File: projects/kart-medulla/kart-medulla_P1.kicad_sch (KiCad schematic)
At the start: 67 parts, among them CN1 1990012, CN10 1990012, CN2 1990012, CN3 1990012, CN4 1990012, CN5 1990012, CN6 1990012, CN7 1990012, CN8 1990012, CN9 1990012, Q3 IRLZ44NPBF, Q4 BSS123_C5184436, U1 LM358DR, U13 MCP4922-E/SL, U14 MAX4660EUA+T, U19 L7805CDT_C20611927, U23 SSW-122-01-T-D, U24 SSW-122-01-T-S, U25 PCF8574T/3,518, U5 SN74LVC3G17DCTR

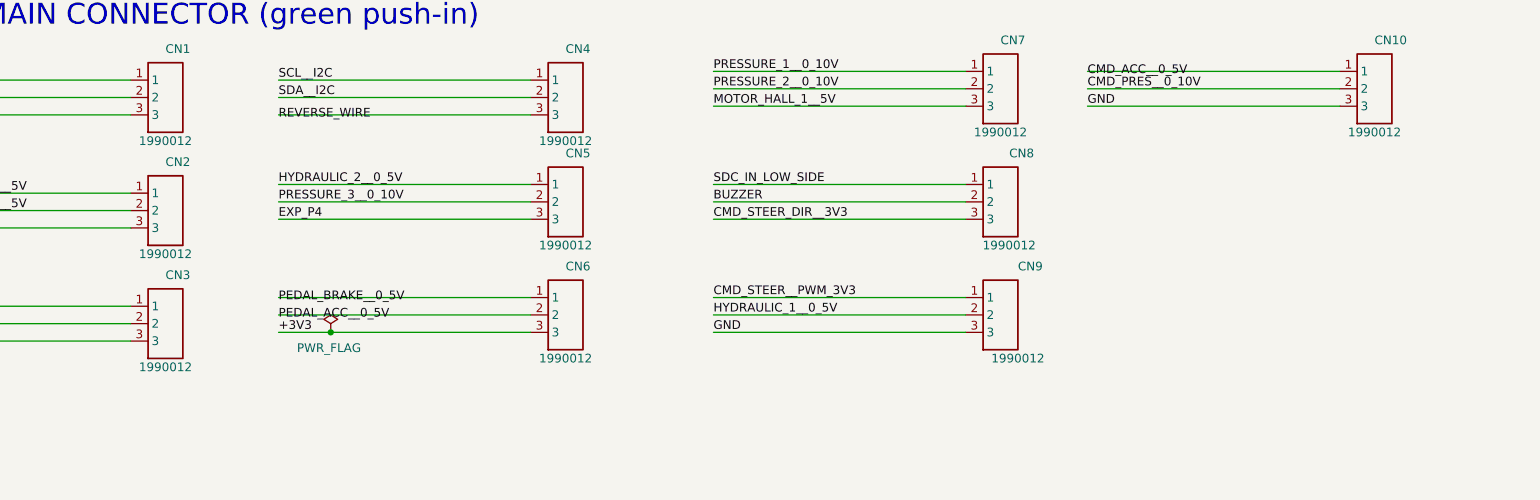
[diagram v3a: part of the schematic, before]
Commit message: swap all ten connectors to the WAGO 2601-3103
CN1-CN10 now use TerminalBlock_WAGO:TerminalBlock_WAGO_2601-3103_1x03_P3.50mm_Vertical
with Value 2601-3103. One connector family, 17.5 A against the Phoenix part's 2 A, top
entry so wires leave upward.

A blind string replace also hit the schematic's cached lib_symbols copy of the symbol,
which made ERC report ten lib_symbol_mismatch warnings because the cache no longer matched
kart-medulla.kicad_sym. Only placed instances carry the new Value; the cached symbol keeps
matching the master. Reverted that one field, ERC back to 0.

The symbol is still named 1990012 after the part it no longer represents - left alone,
since renaming touches the master, the cache and every instance for no electrical gain.

The PCB still has the Phoenix footprints, so parity reports ten more mismatches until the
re-layout.
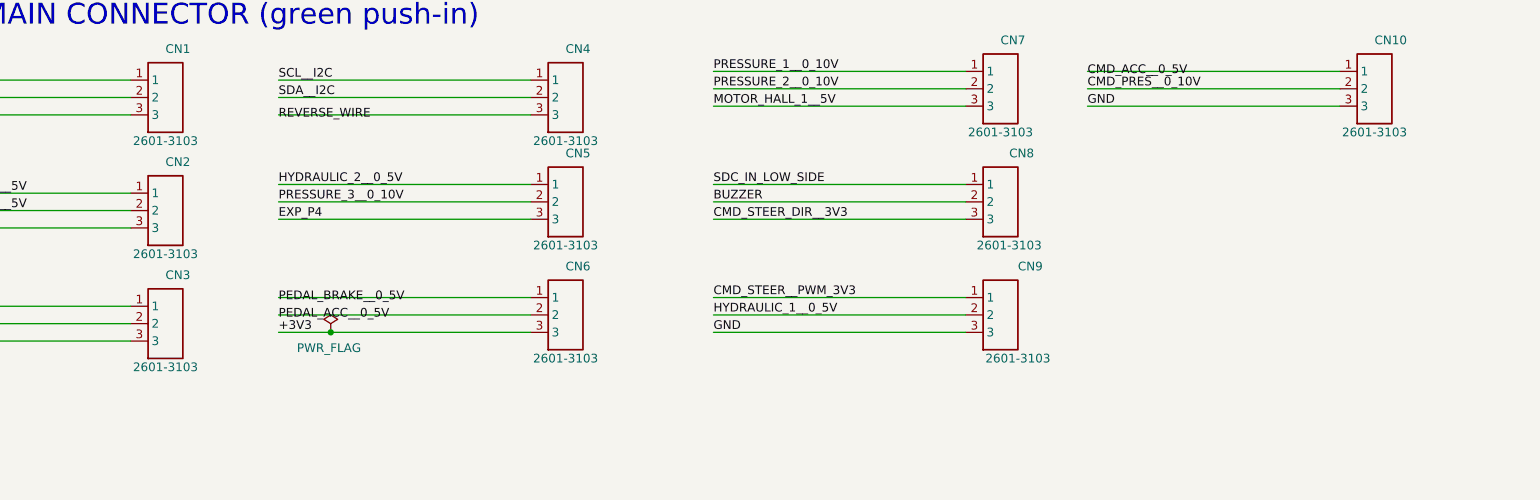
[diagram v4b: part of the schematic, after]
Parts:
- CN1, CN10, CN2, CN3, CN4, CN5, CN6, CN7, CN8, CN9: value 1990012 -> 2601-3103; footprint kart-medulla:CONN-TH_3P-P2.50-S5.00_1990012 -> TerminalBlock_WAGO:TerminalBlock_WAGO_2601-3103_1x03_P3.50mm_Vertical
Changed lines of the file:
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@@
 			)
 		)
-		(property "Value" "1990012"
+		(property "Value" "2601-3103"
 			(at 83.82 72.39 0)
 			(show_name no)
@@
 			)
 		)
-		(property "Footprint" "kart-medulla:CONN-TH_3P-P2.50-S5.00_1990012"
+		(property "Footprint" "TerminalBlock_WAGO:TerminalBlock_WAGO_2601-3103_1x03_P3.50mm_Vertical"
 			(at 83.82 66.04 0)
 			(hide yes)
@@
 			)
 		)
-		(property "Value" "1990012"
+		(property "Value" "2601-3103"
 			(at 83.82 55.88 0)
 			(show_name no)
@@
 			)
 		)
-		(property "Footprint" "kart-medulla:CONN-TH_3P-P2.50-S5.00_1990012"
+		(property "Footprint" "TerminalBlock_WAGO:TerminalBlock_WAGO_2601-3103_1x03_P3.50mm_Vertical"
 			(at 83.82 49.53 0)
 			(hide yes)
@@
 			)
 		)
-		(property "Value" "1990012"
+		(property "Value" "2601-3103"
 			(at 208.28 87.63 0)
 			(show_name no)
@@
 			)
 		)
-		(property "Footprint" "kart-medulla:CONN-TH_3P-P2.50-S5.00_1990012"
+		(property "Footprint" "TerminalBlock_WAGO:TerminalBlock_WAGO_2601-3103_1x03_P3.50mm_Vertical"
 			(at 208.28 81.28 0)
 			(hide yes)
@@
 			)
 		)
-		(property "Value" "1990012"
+		(property "Value" "2601-3103"
 			(at 83.82 88.9 0)
 			(show_name no)
@@
 			)
 		)
-		(property "Footprint" "kart-medulla:CONN-TH_3P-P2.50-S5.00_1990012"
+		(property "Footprint" "TerminalBlock_WAGO:TerminalBlock_WAGO_2601-3103_1x03_P3.50mm_Vertical"
 			(at 83.82 82.55 0)
 			(hide yes)
@@
 			)
 		)
-		(property "Value" "1990012"
+		(property "Value" "2601-3103"
 			(at 142.24 55.88 0)
 			(show_name no)
@@
 			)
 		)
-		(property "Footprint" "kart-medulla:CONN-TH_3P-P2.50-S5.00_1990012"
+		(property "Footprint" "TerminalBlock_WAGO:TerminalBlock_WAGO_2601-3103_1x03_P3.50mm_Vertical"
 			(at 142.24 49.53 0)
 			(hide yes)
@@
 			)
 		)
-		(property "Value" "1990012"
+		(property "Value" "2601-3103"
 			(at 205.74 54.61 0)
 			(show_name no)
@@
 			)
 		)
-		(property "Footprint" "kart-medulla:CONN-TH_3P-P2.50-S5.00_1990012"
+		(property "Footprint" "TerminalBlock_WAGO:TerminalBlock_WAGO_2601-3103_1x03_P3.50mm_Vertical"
 			(at 205.74 48.26 0)
 			(hide yes)
@@
 			)
 		)
-		(property "Value" "1990012"
+		(property "Value" "2601-3103"
 			(at 260.35 54.61 0)
 			(show_name no)
@@
 			)
 		)
-		(property "Footprint" "kart-medulla:CONN-TH_3P-P2.50-S5.00_1990012"
+		(property "Footprint" "TerminalBlock_WAGO:TerminalBlock_WAGO_2601-3103_1x03_P3.50mm_Vertical"
 			(at 260.35 48.26 0)
 			(hide yes)
@@
 			)
 		)
-		(property "Value" "1990012"
+		(property "Value" "2601-3103"
 			(at 142.24 87.63 0)
 			(show_name no)
@@
 			)
 		)
-		(property "Footprint" "kart-medulla:CONN-TH_3P-P2.50-S5.00_1990012"
+		(property "Footprint" "TerminalBlock_WAGO:TerminalBlock_WAGO_2601-3103_1x03_P3.50mm_Vertical"
 			(at 142.24 81.28 0)
 			(hide yes)
@@
 			)
 		)
-		(property "Value" "1990012"
+		(property "Value" "2601-3103"
 			(at 142.24 71.12 0)
 			(show_name no)
@@
 			)
 		)
-		(property "Footprint" "kart-medulla:CONN-TH_3P-P2.50-S5.00_1990012"
+		(property "Footprint" "TerminalBlock_WAGO:TerminalBlock_WAGO_2601-3103_1x03_P3.50mm_Vertical"
 			(at 142.24 64.77 0)
 			(hide yes)
@@
 			)
 		)
-		(property "Value" "1990012"
+		(property "Value" "2601-3103"
 			(at 207.01 71.12 0)
 			(show_name no)
@@
 			)
 		)
-		(property "Footprint" "kart-medulla:CONN-TH_3P-P2.50-S5.00_1990012"
+		(property "Footprint" "TerminalBlock_WAGO:TerminalBlock_WAGO_2601-3103_1x03_P3.50mm_Vertical"
 			(at 207.01 64.77 0)
 			(hide yes)

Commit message: copy the WAGO footprints into the project library so KiCad can resolve them
Update PCB from Schematic removed the Phoenix connectors and could not load the
replacements, because the nickname TerminalBlock_WAGO resolves only through a nested entry
in the global fp-lib-table whose rows use ${KICAD10_FOOTPRINT_DIR} - undefined in this
install (environment.vars is null). My earlier claim that the stock library was reachable
with no setup was wrong in practice.

Copied 2601-3103 and 2601-3102 into kart-medulla.pretty and repointed the ten connectors at
kart-medulla:TerminalBlock_WAGO_2601-3103_1x03_P3.50mm_Vertical. Same form as every other
footprint here, no path variable, no global table, and it keeps the self-contained clone.
Both stock files already declare (attr through_hole).

ERC 0 violations.
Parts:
- CN1, CN10, CN2, CN3, CN4, CN5, CN6, CN7, CN8, CN9: footprint TerminalBlock_WAGO:TerminalBlock_WAGO_2601-3103_1x03_P3.50mm_Vertical -> kart-medulla:TerminalBlock_WAGO_2601-3103_1x03_P3.50mm_Vertical
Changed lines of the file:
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@@
 			)
 		)
-		(property "Footprint" "TerminalBlock_WAGO:TerminalBlock_WAGO_2601-3103_1x03_P3.50mm_Vertical"
+		(property "Footprint" "kart-medulla:TerminalBlock_WAGO_2601-3103_1x03_P3.50mm_Vertical"
 			(at 83.82 66.04 0)
 			(hide yes)
@@
 			)
 		)
-		(property "Footprint" "TerminalBlock_WAGO:TerminalBlock_WAGO_2601-3103_1x03_P3.50mm_Vertical"
+		(property "Footprint" "kart-medulla:TerminalBlock_WAGO_2601-3103_1x03_P3.50mm_Vertical"
 			(at 83.82 49.53 0)
 			(hide yes)
@@
 			)
 		)
-		(property "Footprint" "TerminalBlock_WAGO:TerminalBlock_WAGO_2601-3103_1x03_P3.50mm_Vertical"
+		(property "Footprint" "kart-medulla:TerminalBlock_WAGO_2601-3103_1x03_P3.50mm_Vertical"
 			(at 208.28 81.28 0)
 			(hide yes)
@@
 			)
 		)
-		(property "Footprint" "TerminalBlock_WAGO:TerminalBlock_WAGO_2601-3103_1x03_P3.50mm_Vertical"
+		(property "Footprint" "kart-medulla:TerminalBlock_WAGO_2601-3103_1x03_P3.50mm_Vertical"
 			(at 83.82 82.55 0)
 			(hide yes)
@@
 			)
 		)
-		(property "Footprint" "TerminalBlock_WAGO:TerminalBlock_WAGO_2601-3103_1x03_P3.50mm_Vertical"
+		(property "Footprint" "kart-medulla:TerminalBlock_WAGO_2601-3103_1x03_P3.50mm_Vertical"
 			(at 142.24 49.53 0)
 			(hide yes)
@@
 			)
 		)
-		(property "Footprint" "TerminalBlock_WAGO:TerminalBlock_WAGO_2601-3103_1x03_P3.50mm_Vertical"
+		(property "Footprint" "kart-medulla:TerminalBlock_WAGO_2601-3103_1x03_P3.50mm_Vertical"
 			(at 205.74 48.26 0)
 			(hide yes)
@@
 			)
 		)
-		(property "Footprint" "TerminalBlock_WAGO:TerminalBlock_WAGO_2601-3103_1x03_P3.50mm_Vertical"
+		(property "Footprint" "kart-medulla:TerminalBlock_WAGO_2601-3103_1x03_P3.50mm_Vertical"
 			(at 260.35 48.26 0)
 			(hide yes)
@@
 			)
 		)
-		(property "Footprint" "TerminalBlock_WAGO:TerminalBlock_WAGO_2601-3103_1x03_P3.50mm_Vertical"
+		(property "Footprint" "kart-medulla:TerminalBlock_WAGO_2601-3103_1x03_P3.50mm_Vertical"
 			(at 142.24 81.28 0)
 			(hide yes)
@@
 			)
 		)
-		(property "Footprint" "TerminalBlock_WAGO:TerminalBlock_WAGO_2601-3103_1x03_P3.50mm_Vertical"
+		(property "Footprint" "kart-medulla:TerminalBlock_WAGO_2601-3103_1x03_P3.50mm_Vertical"
 			(at 142.24 64.77 0)
 			(hide yes)
@@
 			)
 		)
-		(property "Footprint" "TerminalBlock_WAGO:TerminalBlock_WAGO_2601-3103_1x03_P3.50mm_Vertical"
+		(property "Footprint" "kart-medulla:TerminalBlock_WAGO_2601-3103_1x03_P3.50mm_Vertical"
 			(at 207.01 64.77 0)
 			(hide yes)

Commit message: rename the DAC-output nets to say 3V3, and fix the docs that still said 0-5 V
Commit 16a35fb moved the MCP4922 U13 from +5V to +3V3 (SPI threshold fix, DS22250A p7) and
raised the LM358 U1A gain from 2 to 3 (R19 1K -> 2K) to keep ~10 V at CN10.2. It did not
update the names and prose downstream that still described the DAC outputs as 0-5 V.

Nets renamed in both the schematic and the PCB:
  CMD_PRES_DAC__0_5V  -> CMD_PRES_DAC__0_3V3
  CMD_ACC_ESP32__0_5V -> CMD_ACC_ESP32__0_3V3

CMD_ACC__0_5V is deliberately unchanged. It is the MAX4660 mux output and carries either the
DAC branch (0-3.3 V) or the driver's pedal (0-5 V), so 0-5 V is its real range.

docs/pinout-esp32-s3.md: the MCP4922 pin table still had VDD, SHDN, VREFA and VREFB on 5 V,
and described VOUTB as "0-5 V at the DAC pin ... amplifies it x2". Now +3V3 and x3, with the
open issue recorded that VOUTA has no gain stage and reaches only ~66% of the motor
controller's 0-5 V input.

parts.md and requirements.md: "LM358 x2 stage" and "MCP4922 DAC (0-5 V)" corrected, with the
resistor values named.

history.md records why R19 reads 2K in the schematic while the fabricated v1 board has 1K
fitted, since that mismatch reads as a regression and is not one.

Also included: in-progress schematic work already in the tree - the throttle buffer stage
(ACC_AMP_OUT / ACC_AMP_FB / CMD_ACC_BUF__0_5V) and the PRESSURE_1/2/3__0_3V3 renames.

ERC 0 violations.
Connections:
- net CMD_ACC_ESP32__0_5V renamed CMD_ACC_ESP32__0_3V3
- net CMD_PRES_DAC__0_5V renamed CMD_PRES_DAC__0_3V3
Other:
- note added: "MAIN CONNECTORS (Wago)"
- note removed: "MAIN CONNECTOR (green push-in)"
